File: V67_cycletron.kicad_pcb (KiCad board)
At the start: 2 copper layers, 102.1 x 110.1 mm, 58 parts, among them J1 USB_C_Receptacle_USB2.0_16P, J3 Screw_Terminal_01x11, U1 LM1117DT-5.0, U2 LM1117DT-3.3, U4 ESP32-S3-WROOM-1

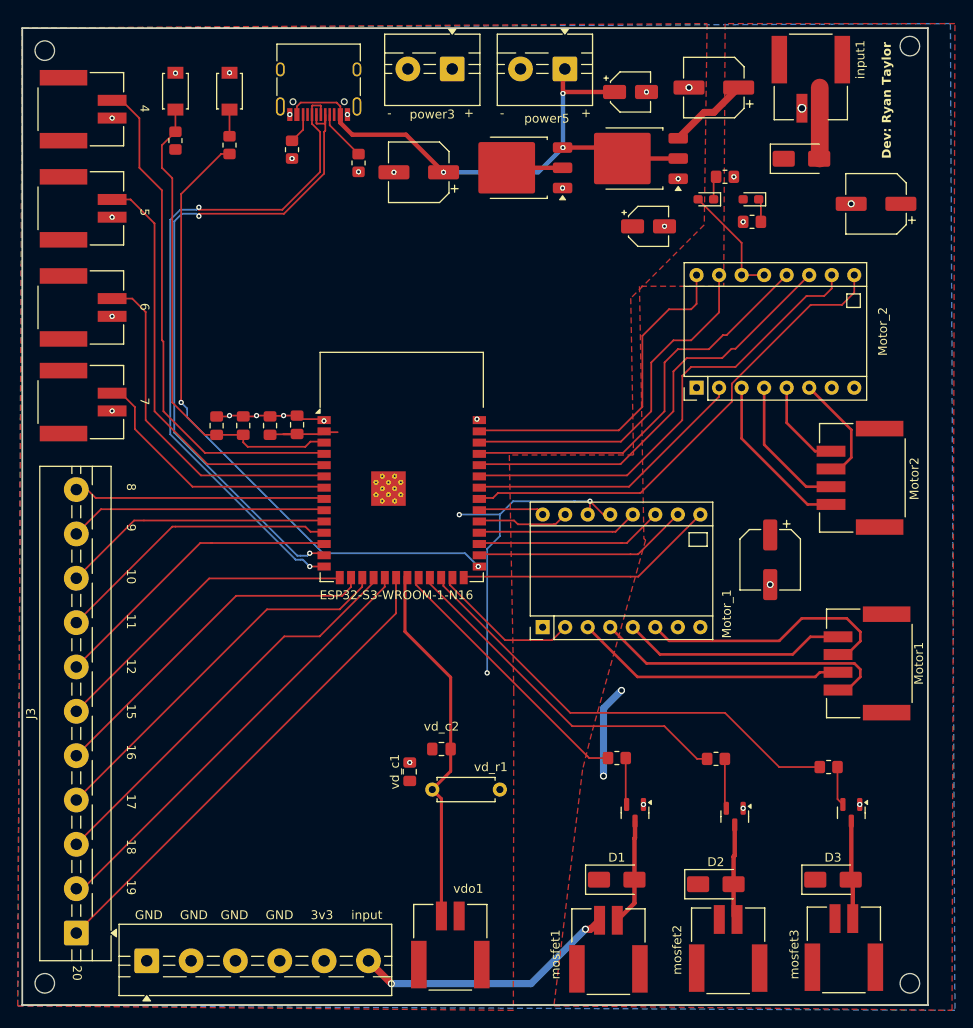
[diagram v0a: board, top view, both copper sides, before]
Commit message: edited silkscreen
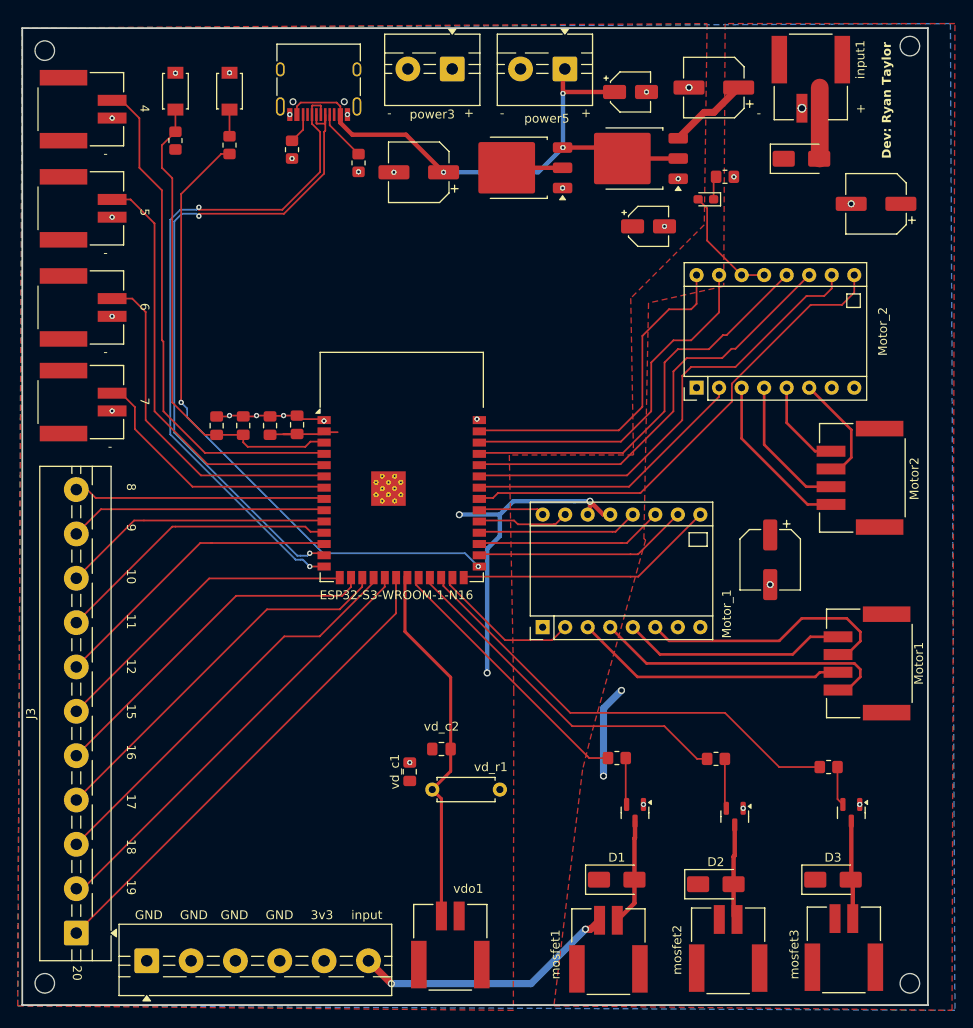
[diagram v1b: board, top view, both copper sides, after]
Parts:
- removed D5: LED, LED_SMD:LED_0603_1608Metric_Pad1.05x0.95mm_HandSolder
- removed R4: 4.7k, Resistor_SMD:R_0805_2012Metric_Pad1.20x1.40mm_HandSolder
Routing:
- net Net-(D5-K): track 2.64 -> 0.00 mm
- net GND: vias 30 -> 29
